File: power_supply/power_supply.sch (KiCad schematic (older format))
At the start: 36 parts, among them J1 Conn_01x04_Male, J2 Conn_01x03_Male, J3 Conn_01x03_Male, J4 Conn_01x03_Male, U1 LM7815_TO220, U2 LM7915_TO220, U3 LM7805_TO220

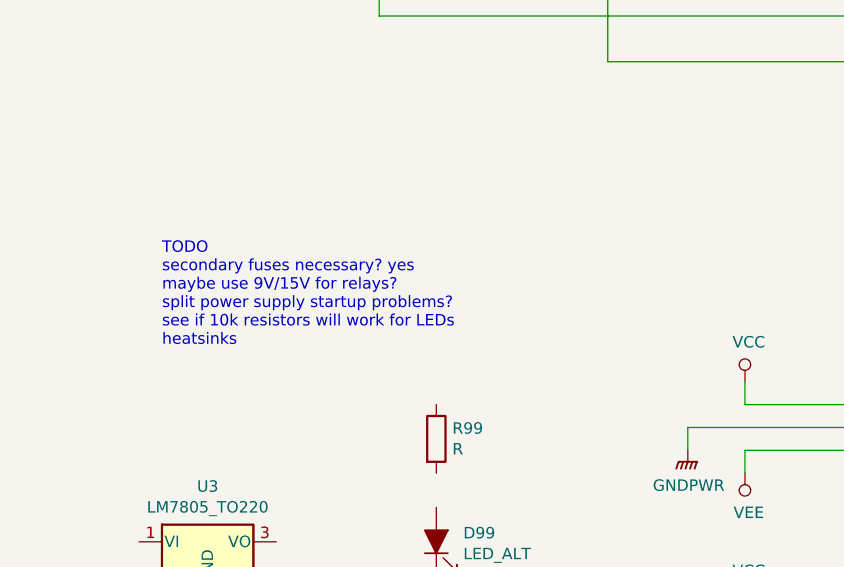
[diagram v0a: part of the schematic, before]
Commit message: add note to change input bypass cap on 7915 to larger electrolytic
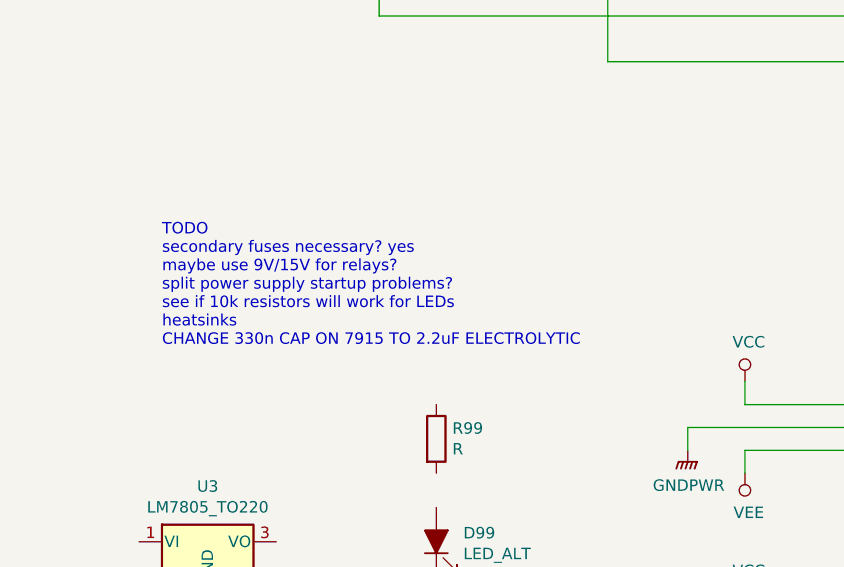
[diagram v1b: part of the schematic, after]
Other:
- note added: "TODO\nsecondary fuses necessary? yes\nmaybe use 9V/15V for relays?\nsplit power supply startup problems?\nsee if 10k resistors will work for LEDs\nheatsinks\nCHANGE 330n CAP ON 7915 TO 2.2uF ELECTROLYTIC"
- note removed: "TODO\nsecondary fuses necessary? yes\nmaybe use 9V/15V for relays?\nsplit power supply startup problems?\nsee if 10k resistors will work for LEDs\nheatsinks"
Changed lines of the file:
@@
 Maybe use 9V or 15V?
 Text Notes 950  4250 0    50   ~ 0
-TODO\nsecondary fuses necessary? yes\nmaybe use 9V/15V for relays?\nsplit power supply startup problems?\nsee if 10k resistors will work for LEDs\nheatsinks
+TODO\nsecondary fuses necessary? yes\nmaybe use 9V/15V for relays?\nsplit power supply startup problems?\nsee if 10k resistors will work for LEDs\nheatsinks\nCHANGE 330n CAP ON 7915 TO 2.2uF ELECTROLYTIC
 $Comp
 L Device:R R2

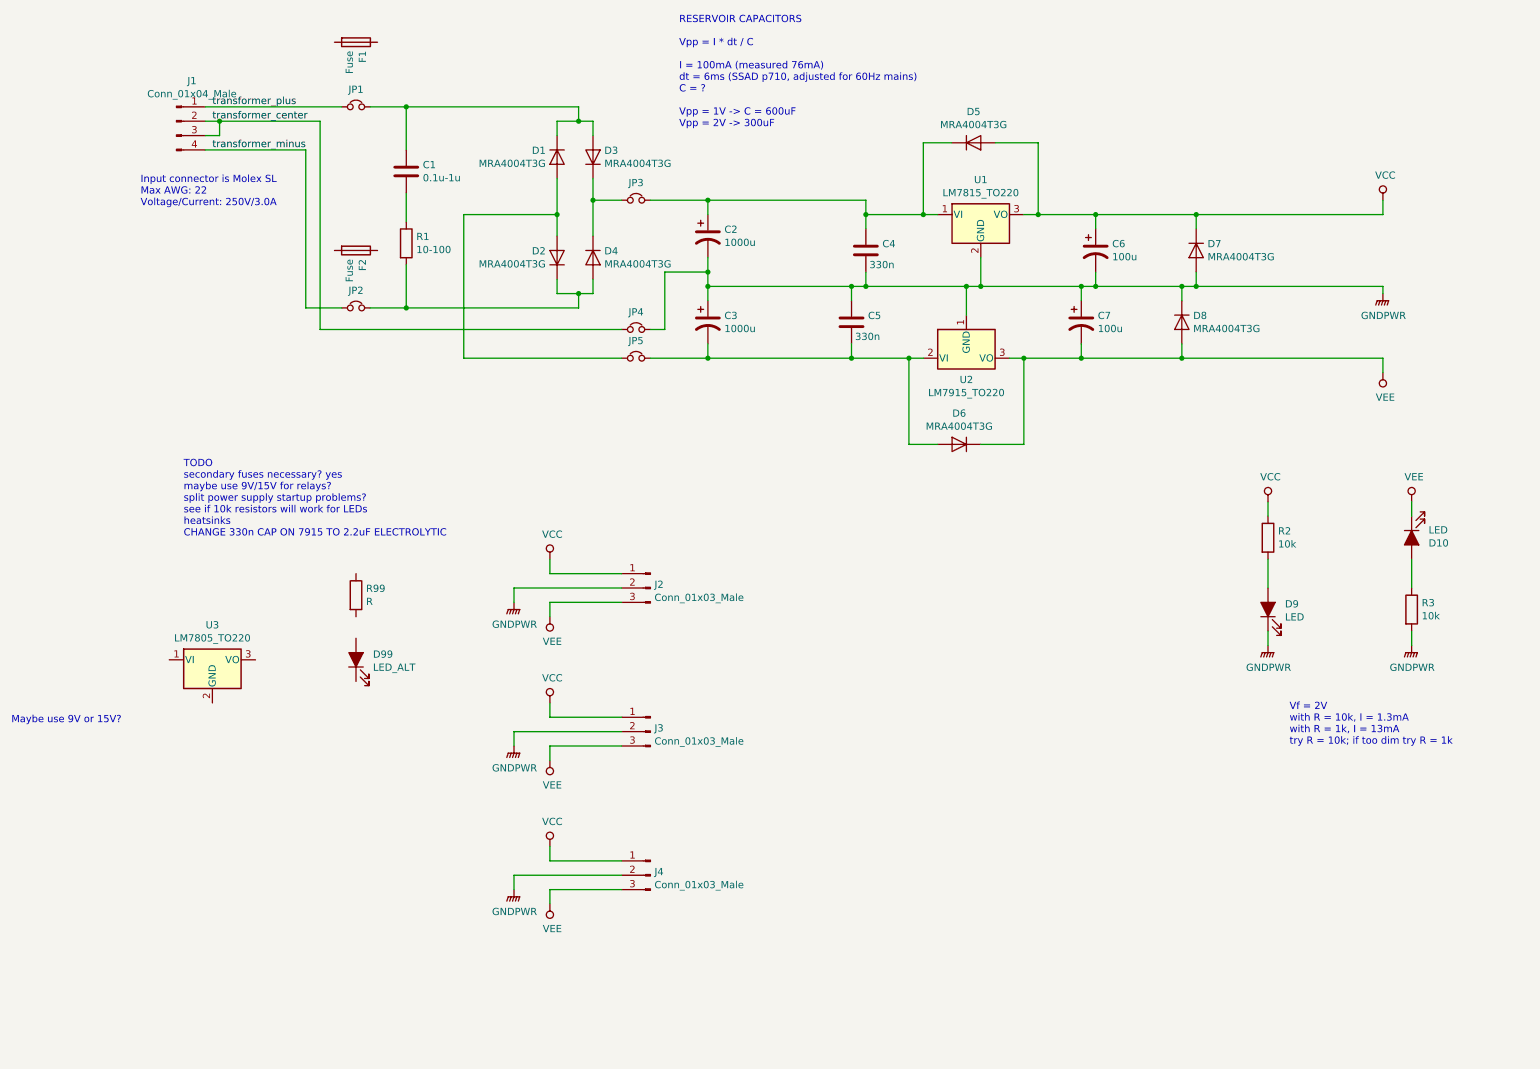
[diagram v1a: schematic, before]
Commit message: Tidy schematic, add additional snubber capacitor
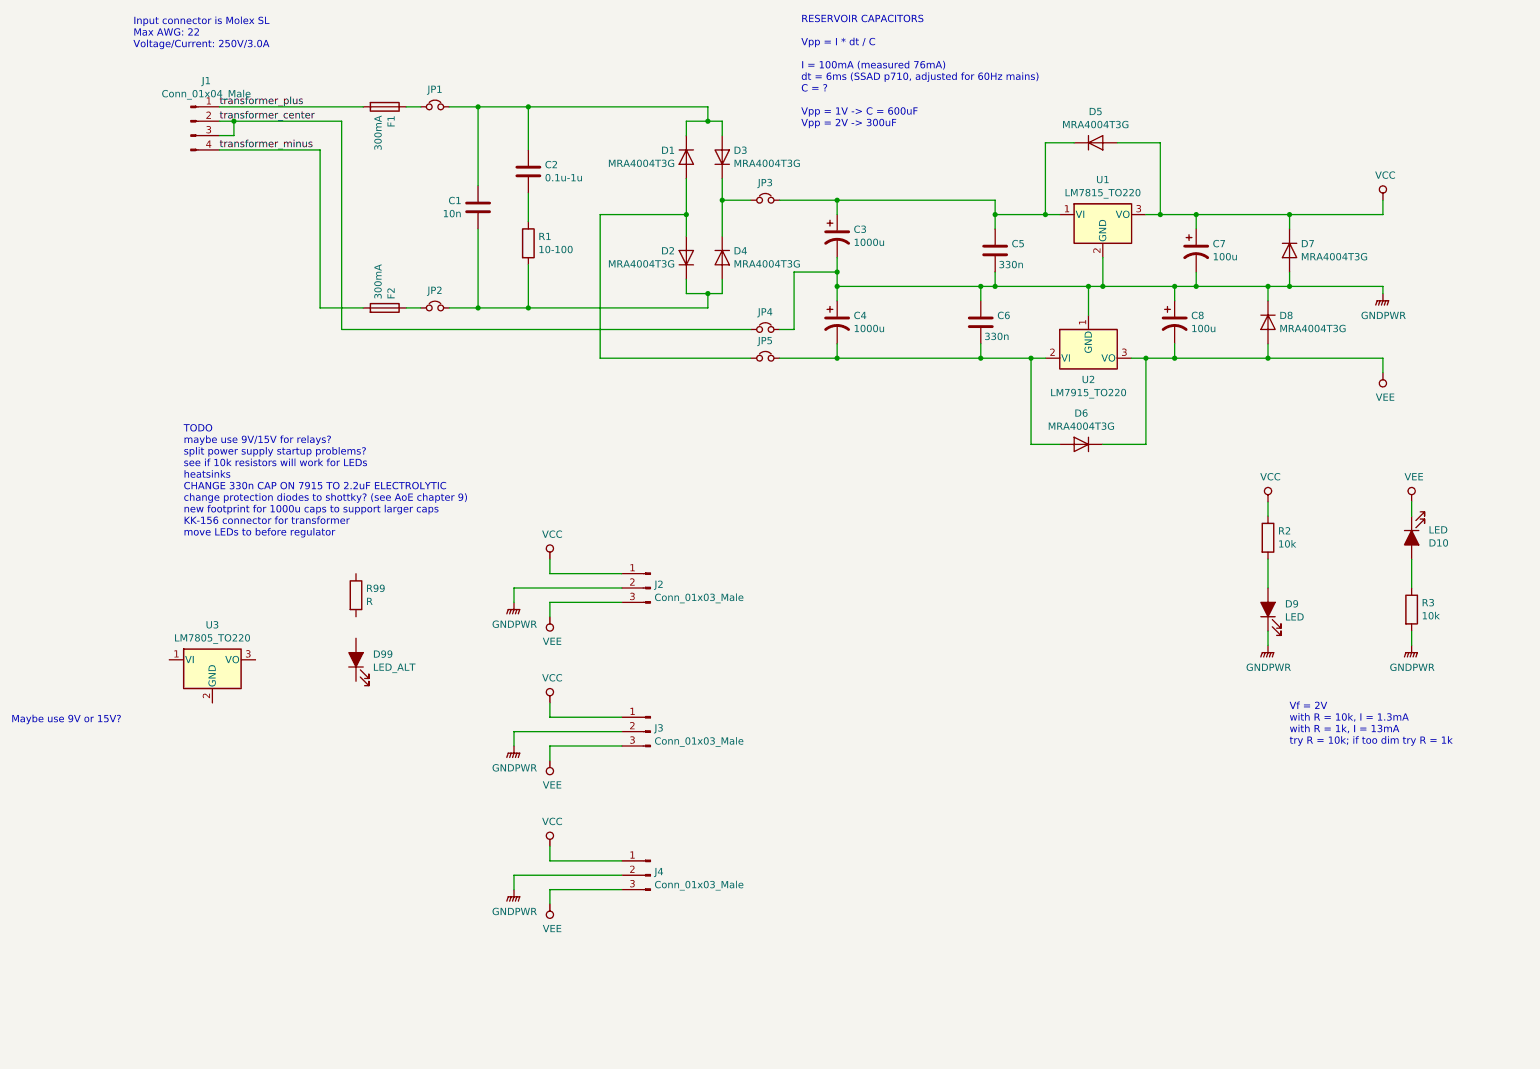
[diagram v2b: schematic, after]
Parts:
- added C1: 10n, symbol Device:C
- F1, F2: value Fuse -> 300mA
- renumbered C1 to C2, C2 to C3, C3 to C4, C4 to C5, C5 to C6, C6 to C7, C7 to C8
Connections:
- net transformer_minus: now also F2.2; no longer JP2.1
- net transformer_plus: now also F1.2; no longer JP1.1
- net at C2.1, D1.1 (K), D3.2 (A)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: now also C1.1
- net at D2.1 (K), D4.2 (A), JP2.2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: now also C1.2
- net at F1.1: now also JP1.1
- net at F2.1: now also JP2.1
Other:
- note added: "TODO\nmaybe use 9V/15V for relays?\nsplit power supply startup problems?\nsee if 10k resistors will work for LEDs\nheatsinks\nCHANGE 330n CAP ON 7915 TO 2.2uF ELECTROLYTIC\nchange protection diodes to shottky? (see AoE chapter 9)\nnew footprint for 1000u caps to support larger caps\nKK-156 connector for transformer\nmove LEDs to before regulator"
- note removed: "TODO\nsecondary fuses necessary? yes\nmaybe use 9V/15V for relays?\nsplit power supply startup problems?\nsee if 10k resistors will work for LEDs\nheatsinks\nCHANGE 330n CAP ON 7915 TO 2.2uF ELECTROLYTIC"
- moved on the sheet: C2, C3, C4, C5, C6, C7, C8, D1, D2, D3, D4, D5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

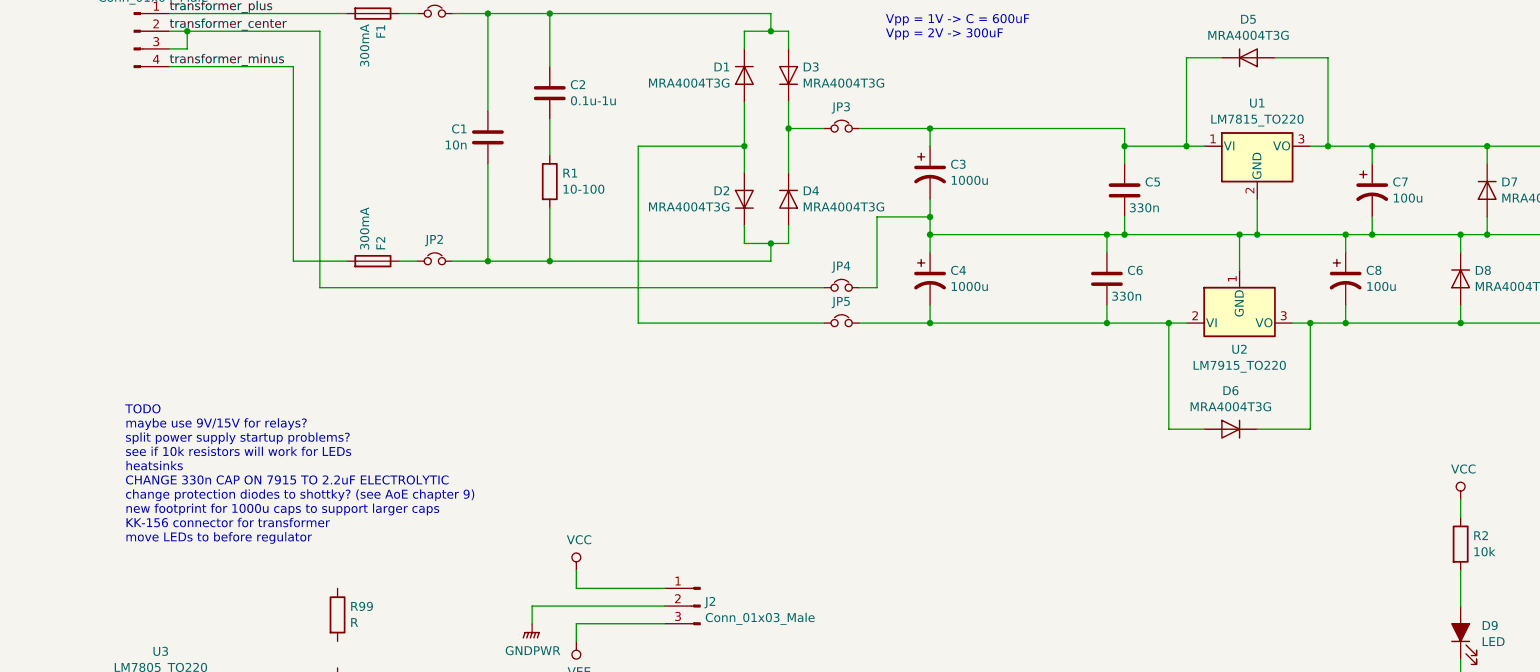
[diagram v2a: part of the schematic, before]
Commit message: update capacitors: add second pair of reservoir caps (DNP) and change input cap to 7915
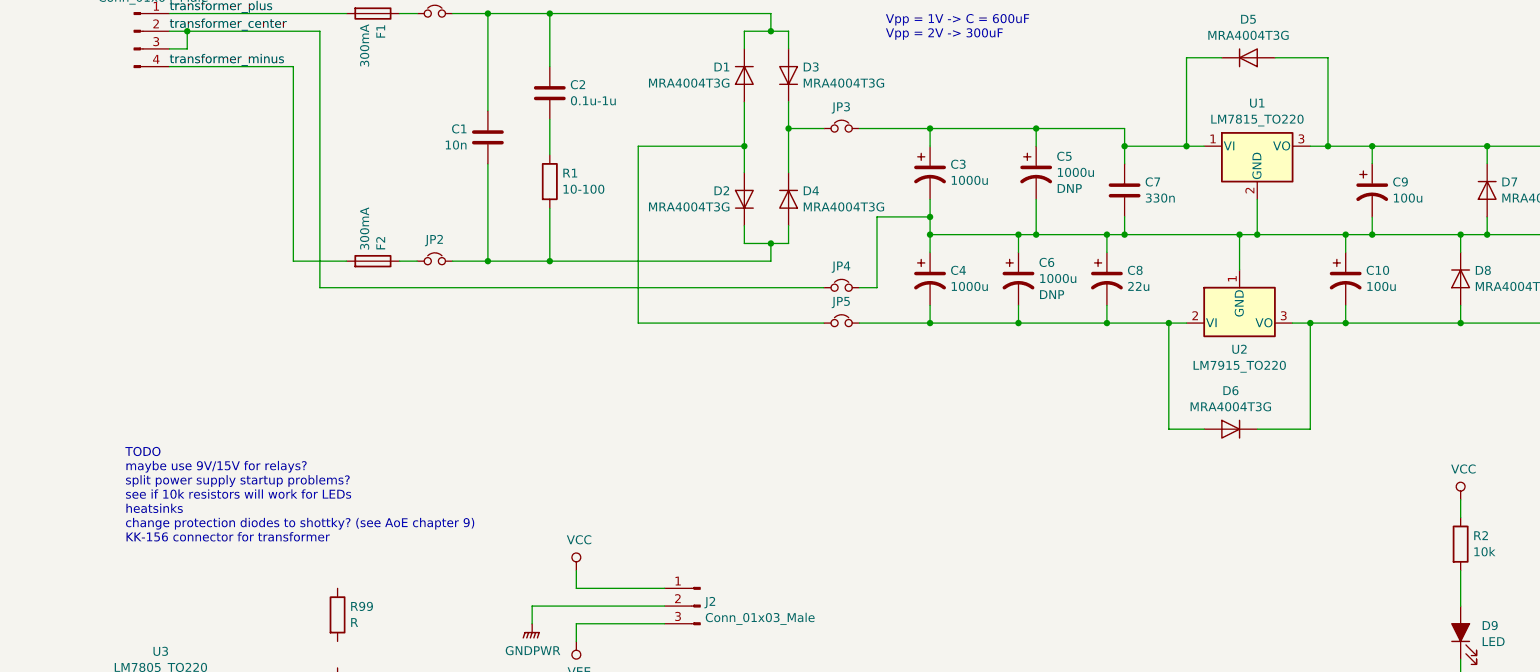
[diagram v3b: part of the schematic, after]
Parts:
- removed C6: 330n, Capacitor_SMD:C_0805_2012Metric_Pad1.15x1.40mm_HandSolder, symbol Device:C
- added C5, C6: 1000u, Capacitor_THT:CP_Radial_D12.5mm_P5.00mm, symbol Device:CP1
- added C8: 22u, Capacitor_THT:CP_Radial_D5.0mm_P2.00mm, symbol Device:CP1
- renumbered C8 to C10, C5 to C7, C7 to C9
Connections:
- net GNDPWR: now also C5.2, C6.1, C8.1
- net at C3.1, C7.1, D5.1 (K)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: now also C5.1
- net at C4.2, D6.2 (A), JP5.2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: now also C6.2, C8.2
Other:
- note added: "TODO\nmaybe use 9V/15V for relays?\nsplit power supply startup problems?\nsee if 10k resistors will work for LEDs\nheatsinks\nchange protection diodes to shottky? (see AoE chapter 9)\nKK-156 connector for transformer"
- note removed: "TODO\nmaybe use 9V/15V for relays?\nsplit power supply startup problems?\nsee if 10k resistors will work for LEDs\nheatsinks\nCHANGE 330n CAP ON 7915 TO 2.2uF ELECTROLYTIC\nchange protection diodes to shottky? (see AoE chapter 9)\nnew footprint for 1000u caps to support larger caps\nKK-156 connector for transformer\nmove LEDs to before regulator"
